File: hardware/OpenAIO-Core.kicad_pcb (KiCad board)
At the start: 6 copper layers, 23 x 20.1 mm, 87 parts, among them J23 5V, J26 5V, J30 5V, J34 5V, J35 5V, J37 5V, J38 5V, J39 5V, J40 5V, J41 5V, J42 5V, J43 5V, J44 5V, J45 5V, J48 5V, J49 5V, J50 5V, J51 5V, J52 5V, J53 5V, J54 5V, J55 5V, J91 Core_LGA, Q1 AP1606, Q2 AP1606, U1 TS2306A 240GF MSM 9_C2976675, U10 COS8051SOT, U11 TLV7031DPWR, U2 RP2354A, U6 LP5912-1.8DRVR, U8 BMI270, U9 SN74LVC1G3157DTBR, X1 XTM25012000JT00351001

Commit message: Circuit: B3 bulk caps and ESP32-C3FH4, LDO caps, BMI270 aux pins, BOOTSEL 1k, unused pads
CIRCUIT_REVIEW B3, S2, S4, S5 and decision D9; LAYOUT_REVIEW 5.3 (pure
clean-up). Values and parts from hardware/KiCad-Library/PARTS-USED.md.

- B3: the 16 +BATT bulk caps had value "C" and no part. C90-C103 (0805)
  4.7uF 50V X5R CL21A475KBQNNNE (C98192, already C18/C19); C105/C106 (1206)
  4.7uF 50V X7R TCC1206X7R475K500HT (C380366, OpenESC).
- D9/B3: U22 is ESP32-C3FH4 (C2858491, in-package flash), as its NC SPI pins
  require; its in-package-flash pads 19, 21-24 deleted per instance (20 was
  already gone). L4 MPN MLZ2012M150WT000 (TDK, SX1281 reference BOM, LCSC not
  in the catalogue); D9 MPN/manufacturer/LCSC from the catalogue.
- S2, LP5912 windows (CIN > 0.5 uF effective, COUT 0.7-10 uF): U7 COUT C28
  22uF -> 1uF CL05A105KA5NQNC; U6 COUT C27 22uF -> 4.7uF CL05A475MP5NRNC;
  U7 CIN C26 100nF -> 1uF GRM033R61A105ME44D in the existing 0201 (an 0402
  does not fit beside U7 without moving parts; ~0.5 uF effective at 4.6 V,
  so it is marginal until U7 moves to the Core in R2, decision S1).
- S4: BMI270 U8 ASDx/ASCx (pins 2/3) were on GND, which the datasheet
  forbids; now +3.3V (VDDIO), valid for the LSM6DSV16X option too.
  Schematic: the GND drop replaced by a +3.3V symbol. Core: pads 2/3 and the
  via between them re-netted, 0.15 mm In3 stub to the In3 +3.3V pour.
- S5: BOOTSEL resistor R7 10k -> 1k (0201WMF1001TEE, C270365): 10k with the
  32k minimum pull-up gave 0.79 V against VIL 0.8 V.
- LAYOUT_REVIEW 5.3, pads on no net with nothing attached: U13/U15/U17/U19
  (AT32F421) 3, 8, 9, 12, 23, 24, 26-28; U14/U16/U18/U20 (NSG2065Q) NC 5, 7,
  8, 21; U7 NC 2; U21 6 (XTB, TCXO), 9, 10 (DIO2/3); Core U2 55-59 (QSPI,
  in-package flash). 60 pads in all; U8 kept for joint symmetry. AT32
  firmware must keep the dropped pins as outputs or pulled.
- Footprint values and fields synced from the schematic for the changed refs.

Deferred: RX LED D9 to +4v5 (S10). +4v5 copper is 1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
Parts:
- C27: value 22uF -> 4.7uF
- R7: value 10k -> 1k
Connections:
- U8 pad 2: GND -> +3.3V
- U8 pad 3: GND -> +3.3V
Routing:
- net +3.3V: track 58.9 -> 59.5 mm, vias 11 -> 12
- net GND: vias 105 -> 104
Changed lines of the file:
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@@
 			)
 		)
-		(property "Value" "22uF"
+		(property "Value" "4.7uF"
 			(at 0 1.16 0)
 			(layer "F.Fab")
@@
 			)
 		)
-		(property "LCSC" "C415703"
+		(property "LCSC" "C23733"
 			(at 0 0 180)
 			(unlocked yes)
@@
 			)
 		)
-		(property "MPN" "GRM155R60J226ME11D"
+		(property "MPN" "CL05A475MP5NRNC"
 			(at 0 0 180)
 			(unlocked yes)
@@
 			)
 		)
-		(property "Manufacturer" "Murata"
+		(property "Manufacturer" "Samsung Electro-Mechanics"
 			(at 0 0 180)
 			(unlocked yes)
@@
 			(size 0.6 0.27)
 			(layers "F.Cu" "F.Mask" "F.Paste")
-			(net "GND")
+			(net "+3.3V")
 			(pinfunction "SDx/AH1/Qvar1_2")
 			(pintype "unspecified")
@@
 			(size 0.6 0.27)
 			(layers "F.Cu" "F.Mask" "F.Paste")
-			(net "GND")
+			(net "+3.3V")
 			(pinfunction "SCx/AH2/Qvar2_3")
 			(pintype "unspecified")
@@
 			(pintype "unspecified")
 		)
-		(pad "55" smd rect
-			(at -0.8 -3.57 180)
-			(size 0.2 0.875)
-			(layers "F.Cu" "F.Mask" "F.Paste")
-			(net "unconnected-(U2-QSPI_SD3-Pad55)")
-			(pinfunction "QSPI_SD3_55")
-			(pintype "unspecified+no_connect")
-		)
-		(pad "56" smd rect
-			(at -1.2 -3.57 180)
-			(size 0.2 0.875)
-			(layers "F.Cu" "F.Mask" "F.Paste")
-			(net "unconnected-(U2-QSPI_SCLK-Pad56)")
-			(pinfunction "QSPI_SCLK_56")
-			(pintype "unspecified+no_connect")
-		)
-		(pad "57" smd rect
-			(at -1.6 -3.57 180)
-			(size 0.2 0.875)
-			(layers "F.Cu" "F.Mask" "F.Paste")
-			(net "unconnected-(U2-QSPI_SD0-Pad57)")
-			(pinfunction "QSPI_SD0_57")
-			(pintype "unspecified+no_connect")
-		)
-		(pad "58" smd rect
-			(at -2 -3.57 180)
-			(size 0.2 0.875)
-			(layers "F.Cu" "F.Mask" "F.Paste")
-			(net "unconnected-(U2-QSPI_SD2-Pad58)")
-			(pinfunction "QSPI_SD2_58")
-			(pintype "unspecified+no_connect")
-		)
-		(pad "59" smd rect
-			(at -2.4 -3.57 180)
-			(size 0.2 0.875)
-			(layers "F.Cu" "F.Mask" "F.Paste")
-			(net "unconnected-(U2-QSPI_SD1-Pad59)")
-			(pinfunction "QSPI_SD1_59")
-			(pintype "unspecified+no_connect")
-		)
 		(pad "60" smd rect
 			(at -2.8 -3.57 180)
@@
 			)
 		)
-		(property "Value" "10k"
+		(property "Value" "1k"
 			(at 0 1.05 90)
 			(layer "F.Fab")
@@
 			)
 		)
-		(property "LCSC" "C106225"
+		(property "LCSC" "C270365"
 			(at 0 0 90)
 			(unlocked yes)
@@
 			)
 		)
-		(property "MPN" "RC0201FR-0710KL"
+		(property "MPN" "0201WMF1001TEE"
 			(at 0 0 90)
 			(unlocked yes)
@@
 			)
 		)
-		(property "Manufacturer" "YAGEO"
+		(property "Manufacturer" "UNI-ROYAL"
 			(at 0 0 90)
 			(unlocked yes)
@@
 	)
 	(via
-		(at 115.61 52.98)
-		(size 0.35)
-		(drill 0.15)
-		(layers "F.Cu" "B.Cu")
-		(net "GND")
-	)
-	(via
 		(at 119.56 59.72)
 		(size 0.35)
@@
 	)
 	(via
+		(at 115.61 52.98)
+		(size 0.35)
+		(drill 0.15)
+		(layers "F.Cu" "B.Cu")
+		(net "+3.3V")
+	)
+	(via
 		(at 108.18 55.82)
 		(size 0.35)
@@
 		(layer "In3.Cu")
 		(net "+3.3V")
+	)
+	(segment
+		(start 115.61 52.98)
+		(end 115 52.98)
+		(width 0.15)
+		(layer "In3.Cu")
+		(net "+3.3V")

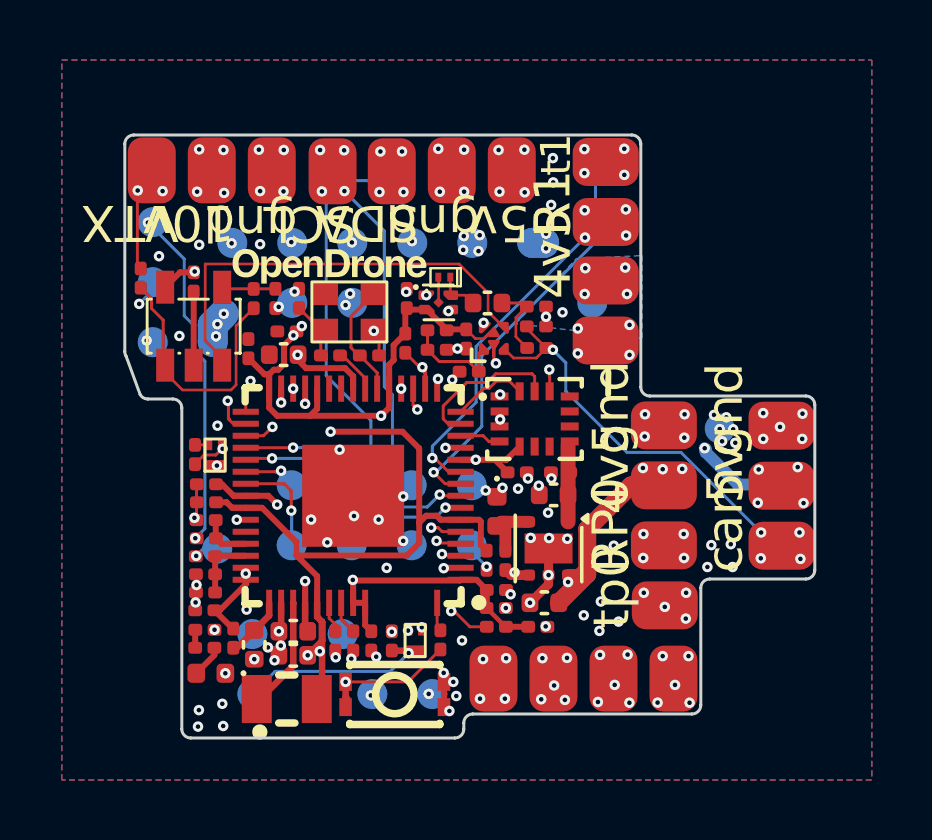
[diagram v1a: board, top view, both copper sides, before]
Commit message: Owner rules: no component silk, pad labels and values, no wordmark text, MPN + maker on every BOM line
The owner rules adopted in PLAN.md (pcb-agent-commons, 2026-10-06), applied
where they are local edits:

- No component silkscreen. J91's reference was the only visible one (Core
  B.Silkscreen, under the LGA) and is hidden. Footprint silk graphics removed
  per instance: Base 234, Core 72. Kept: connector outlines and pin-1 marks
  (USB1, U12 SH-6, Card1, JP1) and the LGA pin-1 marks (J90, J91). Base
  lib_footprint_mismatch warnings 31 -> 40 as a result.
- Solder-pad labels: Core J53 (GND) had none, now "gnd" in the style of J52's
  label. The SH-6 per-pin labels ("10v gnd T0", "R0 gnd R1") become the port
  name "DJI" (connectors: name and pin-1 mark only). Core J48-J51 have no room:
  0.5 mm to J44 above, 0.93 mm to the board edge below. CIRCUIT_REVIEW 8.3
  moves them off the LGA in R2, so their labels go with that move.
- Pad values: all 40 solder-pad symbols said "5V". Each now carries its
  function (5V, GND, LED, BUZ+/BUZ-, 10V, 4V5, CAM, VTX, SCL, SDA, TX0/RX0,
  TX1/RX1, PIO_TX0/PIO_RX0; off-board J19 ADC2, J22 GND, J46/J47 NC).
- No "Drone" text: the "OpenDrone" wordmark on Core F.Silkscreen (9 filled
  polygons in two groups) is removed; a TODO for the incutec wordmark from the
  brand repo sits on User.Comments (not fabricated). No other such text on any
  copper, mask or silk layer of either board.
- BOM: lines missing manufacturer or MPN 41 -> 1. MPNs come from
  PARTS-USED.md by LCSC number. Manufacturers come from the catalogue symbol,
  this design's spelling for the same MPN family, or the committed datasheet
  (NSIC, Sofng, Jiangsu Changjing, Hirose). Still open: Rsense2
  ASR-S-3-0.2F (C695806), whose manufacturer nothing in the catalogue states.
  U24 (board outline) and TP9 (BOOT solder pad) are not parts: excluded from
  BOM and position files.
- 0201 default / minimal capacitance: respected in the circuit commit (C26
  stays 0201; no belt-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
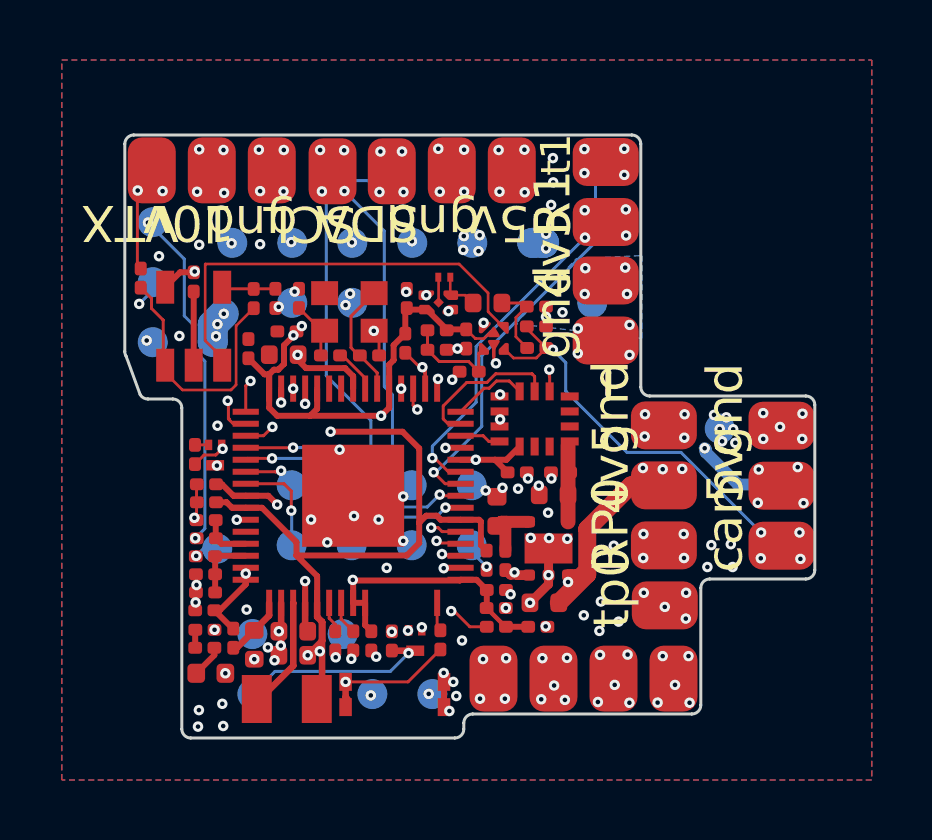
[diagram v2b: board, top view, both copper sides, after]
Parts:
- J23: value 5V -> SCL
- J26: value 5V -> SDA
- J34, J35, J40, J43, J50, J53: value 5V -> GND
- J38: value 5V -> CAM
- J39: value 5V -> VTX
- J41, J51: value 5V -> 10V
- J42, J52: value 5V -> 4V5
- J44: value 5V -> PIO_TX0
- J45: value 5V -> PIO_RX0
- J48: value 5V -> RX0
- J49: value 5V -> TX0
- J54: value 5V -> TX1
- J55: value 5V -> RX1
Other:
- board text added: "TODO brand mark: incutec wordmark from the brand repo (not in R1)"

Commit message: Core: re-route for the 46-pad LGA, B.Cu signal-free, U7 on the Core
New 46-pad J91 land (R2a spec): 25 interface vias in the non-GND pads,
GND vias in the GND pads, U7 (+3.3V LDO) fed from +4v5 on the Core,
+4v5/+5V trunks on In3. All signals on F.Cu/In2/In3 (short In3 hops),
In1/In4 solid GND, B.Cu = LGA pads + GND only. Vias in U2 pins (SCK,
OSD_SYNC, SWDIO, SWCLK, OSD_W, FLASH_CS, UART1_TX) rely on POFV (D4).
28 legacy pad-to-track clearances fixed by narrowing power tracks
(0.20 -> 0.17-0.20) or shifting signal tracks 0.015 mm. Three
fiducials (1 mm / 2 mm mask, board-only, no silk) on F.Cu.

Before (HEAD Core, 34-pad land): DRC 33 clearance errors, parity 255,
94.5 mm of signal track on B.Cu.
Start of this step (46-pad land): DRC 31 clearance, 32 unconnected.
After (refilled, with parity): DRC 0 errors (warnings: 58
lib_footprint_issues), 0 unconnected (pcbnew), parity 206 = 199 Base
footprints + 7 pre-existing pin/pad conflicts, B.Cu signal track 0 mm,
ERC unchanged (31).

Co-Authored-By: Claude Opus 5.5 <noreply@anthropic.com>
Claude-Session: https://claude.ai/code/session_01KTp3FLjVXfXdWrkmr6af7d
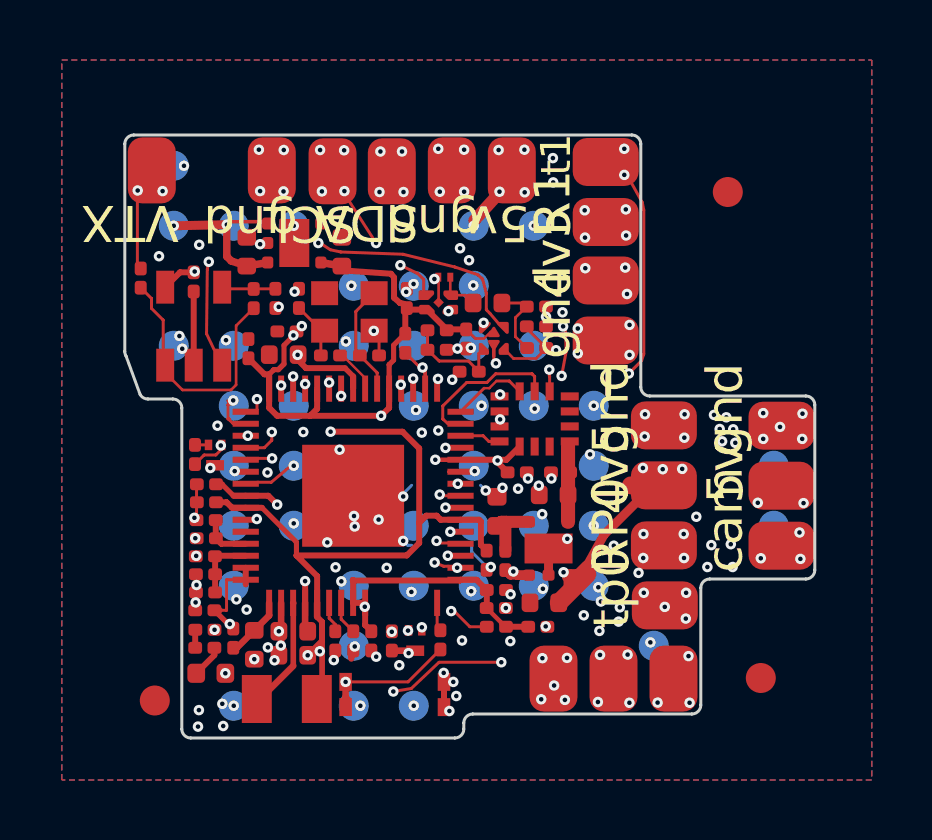
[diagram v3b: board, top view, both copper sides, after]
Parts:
- removed J41, J51: 10V, lib:small_pad
- added C26: 1uF, Capacitor_SMD:C_0402_1005Metric, F.Cu at (107.2, 47.4)
- added C28: 1uF, Capacitor_SMD:C_0402_1005Metric, F.Cu at (110.3, 47.4)
- added FID1: Fiducial_1mm_Mask2mm, Fiducial:Fiducial_1mm_Mask2mm, F.Cu at (104.1, 62.4)
- added FID2: Fiducial_1mm_Mask2mm, Fiducial:Fiducial_1mm_Mask2mm, F.Cu at (124.3, 61.6)
- added FID3: Fiducial_1mm_Mask2mm, Fiducial:Fiducial_1mm_Mask2mm, F.Cu at (123.2, 45.4)
- added U7: LP5912-3.3DRVR, Package_SON:WSON-6-1EP_2x2mm_P0.65mm_EP1x1.6mm, F.Cu at (108.8, 47.1)
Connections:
- J45 pad 1: /Pads/PU0RX -> PU0RX
- J91 pad 1: unconnected-(J91-10V_ENABLE-Pad1) -> GND
- J91 pad 10: GND -> SWDIO
- J91 pad 12: +4v5 -> SPI0.SCK
- J91 pad 13: USB_D- -> SPI0.MOSI
- J91 pad 14: +5V -> GND
- J91 pad 17: MOTOR2 -> SPI0.MISO
- J91 pad 18: MOTOR4 -> GND
- J91 pad 19: GND -> MOTOR3
- J91 pad 2: CURR -> GND
- J91 pad 20: GND -> SWCLK
- J91 pad 21: BUZZER- -> MOTOR4
- J91 pad 22: MOTOR1 -> +5V
- J91 pad 23: MOTOR3 -> MOTOR2
- J91 pad 24: GND -> MOTOR1
- J91 pad 25: GND -> UART1_RX
- J91 pad 26: +BATT -> GND
- J91 pad 29: GND -> FLASH_CS
- J91 pad 3: SPI0.MISO -> +4v5
- J91 pad 30: UART0_TX -> GND
- J91 pad 31: UART0_RX -> GND
- J91 pad 32: LED_STRIP -> GND
- J91 pad 33: UART1_RX -> UART1_TX
- J91 pad 34: UART1_TX -> BUZZER-
- J91 pad 4: SPI0.SCK -> +4v5
- J91 pad 5: SPI0.MOSI -> GND
- J91 pad 6: FLASH_CS -> +5V
- J91 pad 7: +10V -> GND
- J91 pad 8: +3.3V -> CURR
- J91 pad 9: USB_D+ -> GND
- U2 pad 24: unconnected-(U2-SWCLK-Pad24) -> SWCLK
- U2 pad 25: unconnected-(U2-SWDIO-Pad25) -> SWDIO
- U2 pad 5: /Pads/PU0RX -> PU0RX
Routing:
- net +10V: track 18.4 -> 0.00 mm, vias 12 -> 0
- net USB_D+: track 17.3 -> 0.30 mm, vias 2 -> 1
- net PU0RX: track 0.00 -> 14.6 mm, vias 0 -> 9
- net +5V: track 56.5 -> 41.9 mm, vias 12 -> 13
- net +3.3V: track 59.5 -> 46.4 mm, vias 12 -> 11
- net UART1_RX: track 20.9 -> 9.53 mm, vias 6 -> 7
- net USB_D-: track 14.0 -> 2.84 mm
- net /Pads/PU0RX: track 9.25 -> 0.00 mm, vias 5 -> 0
- net +4v5: track 27.3 -> 36.3 mm, vias 9 -> 10
- net UART1_TX: track 23.1 -> 14.9 mm, vias 6 -> 5
- net SPI0.SCK: track 9.85 -> 2.16 mm
- net FLASH_CS: track 9.71 -> 3.09 mm, vias 2 -> 3
- net BUZZER-: track 21.1 -> 14.9 mm, vias 2 -> 3
- net SPI0.MISO: track 7.35 -> 1.34 mm, vias 2 -> 1
- net MOTOR4: track 4.05 -> 9.99 mm, vias 1 -> 3
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- removed copper zone on In3.Cu, net +10V
- removed copper zone on B.Cu, net +4v5
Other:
- board text removed: "10v"

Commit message: DRC: re-enable edge/silk/dangling checks, fix violations from the re-route
Project files: copper_edge_clearance, via_dangling, zones_intersect,
silk_over_copper, silk_edge_clearance -> error, courtyards_overlap ->
warning, Core solder_mask_bridge -> error (were ignore). Counts are
c7f7926 -> this commit, kicad-cli pcb drc --refill-zones
--schematic-parity, new severities.

Base
- copper_edge_clearance 78 -> 4. The 26 +5V tracks/vias from R3-1 that
  ran past the edge (3 wholly outside the outline, which KiCad does not
  report) are re-routed inside: In1 0.3 mm trunk, J16 corner on In1 clear
  of the FID3 0.6 mm keepout, J33 on In2. Every track and via is >= 0.20 mm
  inside Edge.Cuts (shapely check). 51 intended edge pads are named DRU
  exceptions: U24 battery/motor pads 1, 2, 12-23, USB1 shell pad 0,
  J15-J33 lib:small_pad. Left for the owner (pre-existing, need a part
  move): JP1.1 0.37 mm past the 0.20 line, FL1.2 0.19 mm (2.4 GHz filter,
  not moved), U12.7/.8 shell tabs 0.69 mm.
- via_dangling 17 -> 1: 14 introduced vias deleted and their stubs
  trimmed; the one left is in d81e559.
- silk_over_copper 40 -> 34: VTX frame line moved off J41, two U12
  outline segments deleted (owner rule: no component silk), 'DJI' label
  1.0 -> 0.8 mm. The 'Open' logo over the AIO mask text and TP6/TP32 is
  unchanged since d81e559.
- silk_edge_clearance 5 -> 5, clearance 17 -> 17, zones_intersect 0,
  unconnected 0.
- courtyards_overlap (warning; pcbnew count, kicad-cli caps at 199):
  322 -> 323 pairs (d81e559 318). The one introduced real overlap, R113
  (0201) under the U22 QFN body (gap 0.0), is moved to (81.20, 68.65)
  with /RX/BOOT and +3V3 re-routed. No introduced pair is below a 0.15 mm
  body gap now (TP32/TP5 0.19).
- DC, h 0.05: +BATT mean 0.632, GND 0.365 mOhm (c7f7926 0.637 / 0.354
  with +5V outside the board; d81e559 0.729 / 0.445).

Core
- copper_edge_clearance 28 -> 0: UART1_TX, VIDEO_IN and +5V re-routed
  inside the notch, D1 moved 0.025 mm (D1.2 0.186 -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
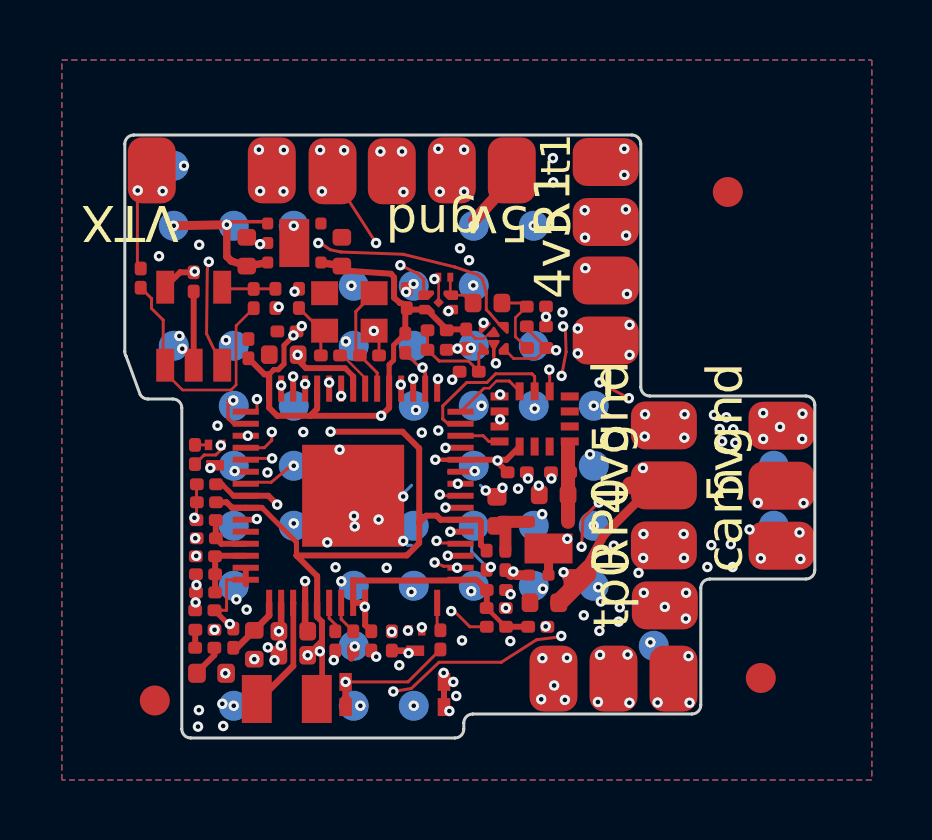
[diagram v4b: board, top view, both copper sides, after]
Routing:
- net +5V: track 41.9 -> 37.4 mm, vias 13 -> 10
- net /OSD/VIDEO_IN: track 13.9 -> 11.6 mm, vias 4 -> 7
- net UART1_TX: track 14.9 -> 15.0 mm, vias 5 -> 4
- net /Pads/I2C0.SDA: vias 8 -> 7
- net /Pads/I2C0.SCL: vias 8 -> 7
- net +4v5: vias 10 -> 7
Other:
- board text removed: "SCL"
- board text removed: "SDA"
